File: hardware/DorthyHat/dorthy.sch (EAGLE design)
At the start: 28 parts, among them J1 90325-0004, J2 90325-0004, U1 DEV-15583

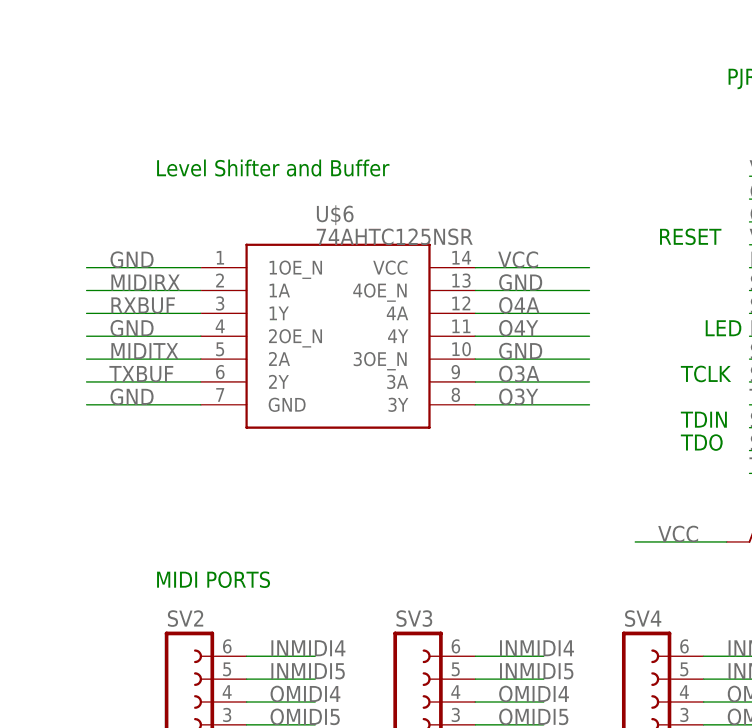
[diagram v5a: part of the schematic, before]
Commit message: Component placement first pass finished for Dorthy
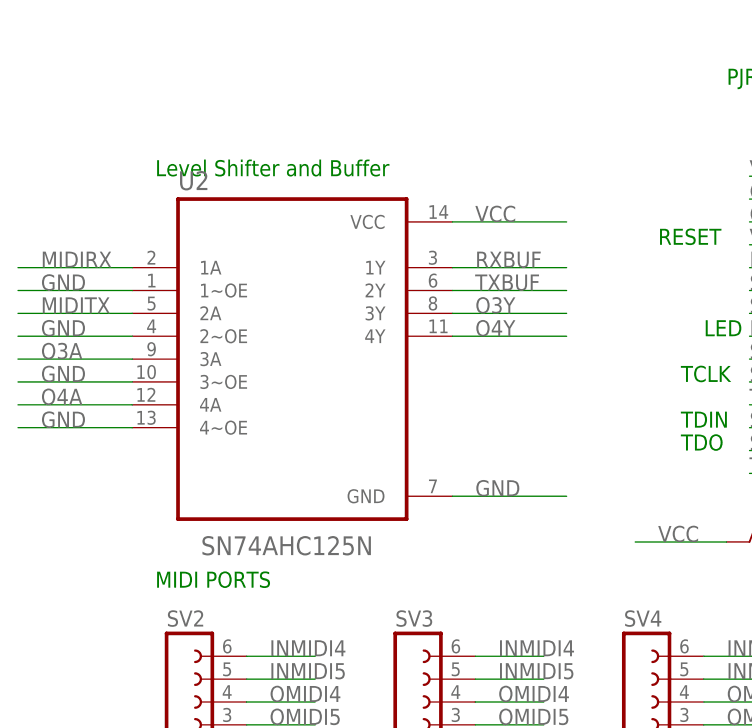
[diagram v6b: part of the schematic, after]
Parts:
- removed U$6: 74AHTC125NSR, DIP794W45P254L1969H508Q14:74AHTC125NSR
- added U2: SN74AHC125N, SN74AHC125N:SN74AHC125N
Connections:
- net GND: now also U2.1~OE, U2.2~OE, U2.3~OE, U2.4~OE, U2.GND; no longer U$6.1OE_N, U$6.2OE_N, U$6.3OE_N, U$6.4OE_N, U$6.GND
- net MIDIRX: now also U2.1A; no longer U$6.1A
- net MIDITX: now also U2.2A; no longer U$6.2A
- net O3A: now also U2.3A; no longer U$6.3A
- net O3Y: now also U2.3Y; no longer U$6.3Y
- net O4A: now also U2.4A; no longer U$6.4A
- net O4Y: now also U2.4Y; no longer U$6.4Y
- net RXBUF: now also U2.1Y; no longer U$6.1Y
- net TXBUF: now also U2.2Y; no longer U$6.2Y
- net VCC: now also U2.VCC; no longer U$6.VCC
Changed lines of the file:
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@@
 <part name="GND1" library="supply1" library_urn="urn:adsk.eagle:library:371" deviceset="GND" device=""/>
 <part name="R2" library="rcl" library_urn="urn:adsk.eagle:library:334" deviceset="R-US_" device="0207/10" package3d_urn="urn:adsk.eagle:package:23491/2" value="470"/>
-<part name="U$6" library="DIP794W45P254L1969H508Q14" deviceset="74AHTC125NSR" device=""/>
 <part name="R3" library="rcl" library_urn="urn:adsk.eagle:library:334" deviceset="R-US_" device="0207/10" package3d_urn="urn:adsk.eagle:package:23491/2" value="220"/>
 <part name="R4" library="rcl" library_urn="urn:adsk.eagle:library:334" deviceset="R-US_" device="0207/10" package3d_urn="urn:adsk.eagle:package:23491/2" value="220"/>
@@
 <part name="U$2" library="Teensy_Audioshield" deviceset="AUDIOSHIELD-REVD" device=""/>
 <part name="U$1" library="ili9341" deviceset="ILI9341" device=""/>
+<part name="U2" library="SN74AHC125N" deviceset="SN74AHC125N" device=""/>
 </parts>
 <sheets>
@@
 <attribute name="VALUE" x="21.082" y="36.83" size="1.778" layer="96" rot="R90"/>
 </instance>
-<instance part="U$6" gate="G$1" x="-109.22" y="129.54" smashed="yes">
-<attribute name="NAME" x="-109.22" y="137.16" size="1.778" layer="95"/>
-<attribute name="VALUE" x="-109.22" y="134.62" size="1.778" layer="96"/>
-</instance>
 <instance part="R3" gate="G$1" x="-50.8" y="25.4" smashed="yes">
 <attribute name="NAME" x="-49.53" y="29.4386" size="1.778" layer="95"/>
@@
 <attribute name="NAME" x="-48.26" y="147.32" size="1.27" layer="95"/>
 <attribute name="VALUE" x="-48.26" y="144.78" size="1.27" layer="96"/>
+</instance>
+<instance part="U2" gate="A" x="-111.76" y="121.92" smashed="yes">
+<attribute name="NAME" x="-124.46" y="140.7" size="2.0828" layer="95" ratio="10" rot="SR0"/>
+<attribute name="VALUE" x="-121.92" y="100.14" size="2.0828" layer="96" ratio="10" rot="SR0"/>
 </instance>
 </instances>
@@
 </segment>
 <segment>
-<wire x1="-78.74" y1="132.08" x2="-91.44" y2="132.08" width="0.1524" layer="91"/>
-<label x="-88.9" y="132.08" size="1.778" layer="95"/>
-<pinref part="U$6" gate="G$1" pin="VCC"/>
-</segment>
-<segment>
 <wire x1="-63.5" y1="25.4" x2="-55.88" y2="25.4" width="0.1524" layer="91"/>
 <pinref part="R3" gate="G$1" pin="1"/>
@@
 <label x="53.34" y="182.88" size="1.778" layer="95"/>
 <pinref part="U$2" gate="G$1" pin="5V"/>
+</segment>
+<segment>
+<wire x1="-81.28" y1="137.16" x2="-93.98" y2="137.16" width="0.1524" layer="91"/>
+<label x="-91.44" y="137.16" size="1.778" layer="95"/>
+<pinref part="U2" gate="A" pin="VCC"/>
 </segment>
 </net>
@@
 </segment>
 <segment>
-<wire x1="-121.92" y1="132.08" x2="-134.62" y2="132.08" width="0.1524" layer="91"/>
-<label x="-132.08" y="132.08" size="1.778" layer="95"/>
-<pinref part="U$6" gate="G$1" pin="1OE_N"/>
-</segment>
-<segment>
-<wire x1="-121.92" y1="116.84" x2="-134.62" y2="116.84" width="0.1524" layer="91"/>
-<label x="-132.08" y="116.84" size="1.778" layer="95"/>
-<pinref part="U$6" gate="G$1" pin="GND"/>
-</segment>
-<segment>
-<wire x1="-121.92" y1="124.46" x2="-134.62" y2="124.46" width="0.1524" layer="91"/>
-<pinref part="U$6" gate="G$1" pin="2OE_N"/>
-<label x="-132.08" y="124.46" size="1.778" layer="95"/>
-</segment>
-<segment>
 <pinref part="J2" gate="G$1" pin="2"/>
 <wire x1="68.58" y1="66.04" x2="50.8" y2="66.04" width="0.1524" layer="91"/>
@@
 </segment>
 <segment>
-<pinref part="U$6" gate="G$1" pin="4OE_N"/>
-<wire x1="-91.44" y1="129.54" x2="-78.74" y2="129.54" width="0.1524" layer="91"/>
-<label x="-88.9" y="129.54" size="1.778" layer="95"/>
-</segment>
-<segment>
-<pinref part="U$6" gate="G$1" pin="3OE_N"/>
-<wire x1="-91.44" y1="121.92" x2="-78.74" y2="121.92" width="0.1524" layer="91"/>
-<label x="-88.9" y="121.92" size="1.778" layer="95"/>
-</segment>
-<segment>
 <wire x1="-48.26" y1="139.7" x2="-60.96" y2="139.7" width="0.1524" layer="91"/>
 <label x="-60.96" y="139.7" size="1.778" layer="95"/>
@@
 <wire x1="5.08" y1="86.36" x2="15.24" y2="86.36" width="0.1524" layer="91"/>
 <label x="7.62" y="86.36" size="1.778" layer="95"/>
+</segment>
+<segment>
+<wire x1="-81.28" y1="106.68" x2="-93.98" y2="106.68" width="0.1524" layer="91"/>
+<label x="-91.44" y="106.68" size="1.778" layer="95"/>
+<pinref part="U2" gate="A" pin="GND"/>
+</segment>
+<segment>
+<wire x1="-129.54" y1="129.54" x2="-142.24" y2="129.54" width="0.1524" layer="91"/>
+<label x="-139.7" y="129.54" size="1.778" layer="95"/>
+<pinref part="U2" gate="A" pin="1~OE"/>
+</segment>
+<segment>
+<wire x1="-129.54" y1="124.46" x2="-142.24" y2="124.46" width="0.1524" layer="91"/>
+<label x="-139.7" y="124.46" size="1.778" layer="95"/>
+<pinref part="U2" gate="A" pin="2~OE"/>
+</segment>
+<segment>
+<wire x1="-129.54" y1="119.38" x2="-142.24" y2="119.38" width="0.1524" layer="91"/>
+<label x="-139.7" y="119.38" size="1.778" layer="95"/>
+<pinref part="U2" gate="A" pin="3~OE"/>
+</segment>
+<segment>
+<wire x1="-129.54" y1="114.3" x2="-142.24" y2="114.3" width="0.1524" layer="91"/>
+<label x="-139.7" y="114.3" size="1.778" layer="95"/>
+<pinref part="U2" gate="A" pin="4~OE"/>
 </segment>
 </net>
@@
 </segment>
 <segment>
-<pinref part="U$6" gate="G$1" pin="1A"/>
-<wire x1="-121.92" y1="129.54" x2="-134.62" y2="129.54" width="0.1524" layer="91"/>
-<label x="-132.08" y="129.54" size="1.778" layer="95"/>
-</segment>
-<segment>
 <wire x1="-22.86" y1="154.94" x2="-10.16" y2="154.94" width="0.1524" layer="91"/>
 <label x="-20.32" y="154.94" size="1.778" layer="95"/>
 <pinref part="U1" gate="G$1" pin="0"/>
+</segment>
+<segment>
+<wire x1="-129.54" y1="132.08" x2="-142.24" y2="132.08" width="0.1524" layer="91"/>
+<label x="-139.7" y="132.08" size="1.778" layer="95"/>
+<pinref part="U2" gate="A" pin="1A"/>
 </segment>
 </net>
@@
 <net name="RXBUF" class="0">
 <segment>
-<pinref part="U$6" gate="G$1" pin="1Y"/>
-<wire x1="-121.92" y1="127" x2="-134.62" y2="127" width="0.1524" layer="91"/>
-<label x="-132.08" y="127" size="1.778" layer="95"/>
-</segment>
-<segment>
 <pinref part="R4" gate="G$1" pin="1"/>
 <wire x1="-63.5" y1="15.24" x2="-55.88" y2="15.24" width="0.1524" layer="91"/>
 <label x="-60.96" y="15.24" size="1.778" layer="95"/>
 </segment>
+<segment>
+<wire x1="-81.28" y1="132.08" x2="-93.98" y2="132.08" width="0.1524" layer="91"/>
+<label x="-91.44" y="132.08" size="1.778" layer="95"/>
+<pinref part="U2" gate="A" pin="1Y"/>
+</segment>
 </net>
 <net name="TXBUF" class="0">
-<segment>
-<wire x1="-121.92" y1="119.38" x2="-134.62" y2="119.38" width="0.1524" layer="91"/>
-<pinref part="U$6" gate="G$1" pin="2Y"/>
-<label x="-132.08" y="119.38" size="1.778" layer="95"/>
-</segment>
 <segment>
 <pinref part="R6" gate="G$1" pin="1"/>
@@
 <label x="-10.16" y="15.24" size="1.778" layer="95"/>
 </segment>
+<segment>
+<wire x1="-81.28" y1="129.54" x2="-93.98" y2="129.54" width="0.1524" layer="91"/>
+<label x="-91.44" y="129.54" size="1.778" layer="95"/>
+<pinref part="U2" gate="A" pin="2Y"/>
+</segment>
 </net>
 <net name="TMIDI4" class="0">
@@
 <net name="MIDITX" class="0">
 <segment>
-<wire x1="-121.92" y1="121.92" x2="-134.62" y2="121.92" width="0.1524" layer="91"/>
-<pinref part="U$6" gate="G$1" pin="2A"/>
-<label x="-132.08" y="121.92" size="1.778" layer="95"/>
-</segment>
-<segment>
 <wire x1="-10.16" y1="152.4" x2="-22.86" y2="152.4" width="0.1524" layer="91"/>
 <label x="-20.32" y="152.4" size="1.778" layer="95"/>
 <pinref part="U1" gate="G$1" pin="1"/>
 </segment>
-</net>
-<net name="O3A" class="0">
-<segment>
-<pinref part="U$6" gate="G$1" pin="3A"/>
-<wire x1="-91.44" y1="119.38" x2="-78.74" y2="119.38" width="0.1524" layer="91"/>
-<label x="-88.9" y="119.38" size="1.778" layer="95"/>
-</segment>
-</net>
-<net name="O3Y" class="0">
-<segment>
-<pinref part="U$6" gate="G$1" pin="3Y"/>
-<wire x1="-91.44" y1="116.84" x2="-78.74" y2="116.84" width="0.1524" layer="91"/>
-<label x="-88.9" y="116.84" size="1.778" layer="95"/>
-</segment>
-</net>
-<net name="O4Y" class="0">
-<segment>
-<pinref part="U$6" gate="G$1" pin="4Y"/>
-<wire x1="-91.44" y1="124.46" x2="-78.74" y2="124.46" width="0.1524" layer="91"/>
-<label x="-88.9" y="124.46" size="1.778" layer="95"/>
-</segment>
-</net>
-<net name="O4A" class="0">
-<segment>
-<pinref part="U$6" gate="G$1" pin="4A"/>
-<wire x1="-91.44" y1="127" x2="-78.74" y2="127" width="0.1524" layer="91"/>
-<label x="-88.9" y="127" size="1.778" layer="95"/>
+<segment>
+<wire x1="-129.54" y1="127" x2="-142.24" y2="127" width="0.1524" layer="91"/>
+<label x="-139.7" y="127" size="1.778" layer="95"/>
+<pinref part="U2" gate="A" pin="2A"/>
 </segment>
 </net>
@@
 </segment>
 </net>
+<net name="O3A" class="0">
+<segment>
+<wire x1="-142.24" y1="121.92" x2="-129.54" y2="121.92" width="0.1524" layer="91"/>
+<label x="-139.7" y="121.92" size="1.778" layer="95"/>
+<pinref part="U2" gate="A" pin="3A"/>
+</segment>
+</net>
+<net name="O4A" class="0">
+<segment>
+<wire x1="-142.24" y1="116.84" x2="-129.54" y2="116.84" width="0.1524" layer="91"/>
+<label x="-139.7" y="116.84" size="1.778" layer="95"/>
+<pinref part="U2" gate="A" pin="4A"/>
+</segment>
+</net>
+<net name="O3Y" class="0">
+<segment>
+<wire x1="-93.98" y1="127" x2="-81.28" y2="127" width="0.1524" layer="91"/>
+<label x="-91.44" y="127" size="1.778" layer="95"/>
+<pinref part="U2" gate="A" pin="3Y"/>
+</segment>
+</net>
+<net name="O4Y" class="0">
+<segment>
+<wire x1="-93.98" y1="124.46" x2="-81.28" y2="124.46" width="0.1524" layer="91"/>
+<label x="-91.44" y="124.46" size="1.778" layer="95"/>
+<pinref part="U2" gate="A" pin="4Y"/>
+</segment>
+</net>
